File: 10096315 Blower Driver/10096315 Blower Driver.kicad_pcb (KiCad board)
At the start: 4 copper layers, 0 parts

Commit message: Created KiCad PCB Fie from Source
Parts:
- added ?: , , F.Cu at (266.1, 17.3)
- added ?: , , F.Cu at (266.6, 36.6)
- added ?: , , F.Cu at (278.6, 36.6)
- added ?: , , F.Cu at (290.4, 36.6)
- added ?: , , F.Cu at (291.6, 19.9)
- added ?: , , F.Cu at (295.0, 19.4)
- added C1: C-BC-C0805, C0805_1, F.Cu at (258.4, 23.7)
- added C10: C-BC-C1206, RC1206_1, F.Cu at (271.8, 63.4)
- added C11: C-BC-C0603, C0603_1, F.Cu at (267.0, 66.3)
- added C12: C-BC-C0805, C0805_2, F.Cu at (288.3, 57.7)
- added C13: C-BC-C1206, RC1206_1, F.Cu at (283.8, 63.4)
- added C14: C-BC-C0603, C0603_1, F.Cu at (279.1, 66.3)
- added C15: C-BC-C0805, C0805_2, F.Cu at (300.3, 57.7)
- added C16: C-BC-C1206, RC1206_1, F.Cu at (295.6, 63.4)
- added C17: C-BC-C0603, C0603_1, F.Cu at (290.8, 66.3)
- added C18: C-BC-C0805, C0805_1, F.Cu at (326.7, 40.2)
- added C19: C-BC-C0805, C0805_2, F.Cu at (309.6, 47.2)
- added C2: C-BTP-803, 03515_1, F.Cu at (305.8, 19.3)
- added C20: C-BC-C0603, C0603_1, F.Cu at (326.7, 42.5)
- added C21: C-BC-C0805, C0805_1, F.Cu at (317.8, 37.7)
- added C22: CC-BC-C0612, C0612-4_1, F.Cu at (299.4, 11.7)
- added C23: CC-BC-C0612, C0612-4_1, F.Cu at (309.2, 11.7)
- added C24: C-BC-C0805, C0805_1, F.Cu at (274.0, 45.3)
- added C25: C-BC-C0805, C0805_1, F.Cu at (286.1, 45.3)
- added C26: C-BC-C0805, C0805_1, F.Cu at (298.1, 45.3)
- added C27: C-BTP-803, 03515_1, F.Cu at (305.8, 30.1)
- added C28: C-BTP-HT1327, HT-13X27_1, F.Cu at (267.8, 19.5)
- added C29: C-BTP-HT1327, HT-13X27_1, F.Cu at (267.8, 6.51)
- added C3: C-BC-C0805, C0805_2, F.Cu at (299.1, 24.1)
- added C4: C-BCP-C7343, C7343_1, F.Cu at (271.8, 28.8)
- added C5: C-BC-C0805, C0805_2, F.Cu at (297.2, 28.8)
- added C6: C-BC-C0805, C0805_2, F.Cu at (315.9, 64.7)
- added C7: C-BC-C0603, C0603_1, F.Cu at (309.6, 59.6)
- added C8: C-BC-C0603, C0603_1, F.Cu at (309.6, 57.7)
- added C9: C-BC-C0805, C0805_2, F.Cu at (276.2, 57.7)
- added CAM14: FEE_COMP, FEE_COMP_1, B.Cu at (247.0, 71.1)
- added CAM15: FEE_COMP, FEE_COMP_1, F.Cu at (315.0, 71.1)
- added CAM5: FILM18_HORIZONTAL, FILM18_HORIZONTAL_1, F.Cu at (288.3, 42.0)
- added D1: D-BC-SMB, SMB_1, F.Cu at (291.5, 28.2)
- added D10: D-BC-SMA, SMA_1, F.Cu at (288.6, 51.4)
- added D11: D-BC-SOD80, SOD80_1, F.Cu at (271.8, 66.3)
- added D12: D-BC-SOD80, SOD80_1, F.Cu at (283.8, 66.3)
- added D13: D-BC-SOD80, SOD80_1, F.Cu at (295.6, 66.3)
- added D14: D-BC-SOT23, SOT23-1G_1, F.Cu at (267.0, 63.4)
- added D15: D-BC-SOT23, SOT23-1G_1, F.Cu at (279.1, 63.4)
- added D16: D-BC-SOT23, SOT23-1G_1, F.Cu at (290.8, 63.4)
- added D17: D-BC-DPAK-2ANODES, DPAK-2ANODES_1, B.Cu at (274.3, 11.4)
- added D18: D-BC-SMB, SMB_1, F.Cu at (268.3, 45.3)
- added D19: D-BC-SMB, SMB_2, F.Cu at (270.8, 37.1)
- added D2: D-BC-SOD323, SOD323_1, F.Cu at (270.8, 60.3)
- added D20: D-BC-SMB, SMB_1, F.Cu at (280.4, 45.3)
- added D21: D-BC-SMB, SMB_2, F.Cu at (282.9, 37.1)
- added D22: D-BC-SMB, SMB_1, F.Cu at (292.4, 45.3)
- added D23: D-BC-SMB, SMB_2, F.Cu at (295.0, 37.1)
- added D24: D-BC-SOT23, SOT23-1G_2, F.Cu at (285.7, 28.5)
- added D3: D-BC-SOD323, SOD323_1, F.Cu at (282.9, 60.3)
- added D4: D-BC-SOD323, SOD323_1, F.Cu at (295.0, 60.3)
- added D5: D-BC-SOD323, SOD323_1, F.Cu at (273.0, 33.6)
- added D6: D-BC-SOD323, SOD323_1, F.Cu at (284.8, 33.6)
- added D7: D-BC-SOD323, SOD323_1, F.Cu at (296.9, 33.6)
- added D8: D-BC-SMA, SMA_1, F.Cu at (265.1, 51.0)
- added D9: D-BC-SMA, SMA_1, F.Cu at (276.5, 51.0)
- added F1: FU-BC-154000, FU154000_1, F.Cu at (261.0, 28.8)
- added FI1: FL-10-BNX002-01, BNX002_1, F.Cu at (248.9, 26.0)
- added FI3: SF-BC-S0603, C0603_1, F.Cu at (302.9, 11.4)
- added FI4: SF-BC-S0603, C0603_1, F.Cu at (304.8, 11.4)
- added FI5: SF-BC-S0603, C0603_1, F.Cu at (306.7, 11.4)
- added FI6: SF-BC-S0603, C0603_1, F.Cu at (319.1, 11.4)
- added FI7: SF-BC-S0603, C0603_1, F.Cu at (317.2, 11.4)
- added FI8: SF-BC-S0603, C0603_1, F.Cu at (315.3, 11.4)
- added FI9: SF-BC-S0603, C0603_1, F.Cu at (313.4, 11.4)
- added IC1: L-BC-SO24, MX.A24_COMPOSANT_1, F.Cu at (317.8, 47.6)
- added IC2: L-BC-SO08, MX.A8_COMPOSANT_1, F.Cu at (315.9, 60.6)
- added IC3: L-BC-SO08, MX.A8_COMPOSANT_1, F.Cu at (270.5, 56.1)
- added IC4: L-BC-SO08, MX.A8_COMPOSANT_1, F.Cu at (282.6, 56.1)
- added IC5: L-BC-SO08, MX.A8_COMPOSANT_1, F.Cu at (294.6, 56.1)
- added IC6: REG-BC-DPAK, DPAK_1, B.Cu at (292.7, 10.1)
- added J1: F-COCMS-MOL43650-0212, MOL43650-02C_1, F.Cu at (261.3, 19.7)
- added J11: F-CO-MOL5566-02, MOL5566-2_1, F.Cu at (243.8, 16.7)
- added J2: F-CO-HE10-2010D, BP2X5D_1, F.Cu at (314.8, 4.05)
- added J22: F-CO-MOL7395M09, MOL7395-9_1, F.Cu at (313.8, 14.2)
- added J3: F-CO-MOL7395M02, MOL7395-2_1, F.Cu at (261.3, 56.4)
- added J6: F-CO-MOL7395M08, MOL7395-8_1, F.Cu at (261.3, 51.4)
- added MIR1: MIRECMS, MIRECMS-SAFT_1, F.Cu at (243.8, 2.47)
- added MIR2: MIRECMS, MIRECMS-SAFT_1, F.Cu at (330.5, 69.1)
- added MIR3: MIRECMS, MIRECMS-SAFT_1, B.Cu at (331.5, 5.32)
- added MIR4: MIRECMS, MIRECMS-SAFT_1, B.Cu at (249.9, 69.8)
- added PT1: PT-CMS-C12000, C12000_1, F.Cu at (328.9, 2.14)
- added R1: R-BC-R2512, R2512_1, F.Cu at (305.4, 42.1)
- added R10: R-BC-R0603, R0603_1, F.Cu at (295.6, 69.1)
- added R11: R-BC-R0603, R0603_1, F.Cu at (267.3, 60.3)
- added R12: R-BC-R0603, R0603_1, F.Cu at (279.4, 60.3)
- added R13: R-BC-R0603, R0603_1, F.Cu at (291.5, 60.3)
- added R2: R-BC-R0603, R0603_1, F.Cu at (309.6, 49.5)
- added R20: R-BC-R0603, R0603_1, F.Cu at (295.0, 52.3)
- added R3: R-BC-R0603, R0603_1, F.Cu at (278.1, 27.5)
- added R30: R-BC-R0603, R0603_1, F.Cu at (293.1, 33.6)
- added R31: R-BC-R0603, R0603_1, F.Cu at (269.2, 33.6)
- added R32: R-BC-R0603, R0603_1, F.Cu at (282.9, 52.3)
- added R33: R-BC-R0603, R0603_1, F.Cu at (281.0, 33.6)
- added R35: R-BC-R0603, R0603_1, F.Cu at (270.8, 52.3)
- added R37: R-BC-R0603, R0603_1, F.Cu at (309.6, 61.5)
- added R38: R-BC-R0603, R0603_1, F.Cu at (305.4, 45.3)
- added R39: R-BC-R0603, R0603_1, F.Cu at (311.8, 37.7)
- added R4: R-BC-R0603, R0603_1, F.Cu at (266.1, 23.7)
- added R40: R-BC-R2512, R2512_1, F.Cu at (305.4, 38.0)
- added R41: R-BC-R0603, R0603_1, F.Cu at (326.7, 44.7)
- added R42: R-BC-R0603, R0603_1, F.Cu at (326.7, 38.0)
- added R5: R-BC-R0603, R0603_1, F.Cu at (326.7, 46.6)
- added R50: R-BC-R0603, R0603_1, F.Cu at (309.6, 63.4)
- added R58: R-BC-R1206, RC1206_1, F.Cu at (275.3, 60.3)
- added R59: R-BC-R1206, RC1206_1, F.Cu at (287.3, 60.3)
- added R6: R-BC-R0603, R0603_1, F.Cu at (271.8, 69.1)
- added R60: R-BC-R1206, RC1206_1, F.Cu at (299.4, 60.3)
- added R7: R-BC-R0603, R0603_1, F.Cu at (329.6, 38.0)
- added R8: R-BC-R0603, R0603_1, F.Cu at (326.7, 48.5)
- added R9: R-BC-R0603, R0603_1, F.Cu at (283.8, 69.1)
- added T1: Q-SOT23-IRLML2803, SOT23-GSD_1, F.Cu at (309.6, 53.3)
- added T10: Q-SOT23-IRLML2803, SOT23-GSD_2, F.Cu at (281.9, 28.5)
- added T2: Q-BC-DPAK-GDS, DPAK-GDS_1, B.Cu at (270.5, 58.7)
- added T3: Q-BC-DPAK-GDS, DPAK-GDS_1, B.Cu at (270.5, 31.7)
- added T4: Q-BC-DPAK-GDS, DPAK-GDS_1, B.Cu at (282.6, 58.7)
- added T5: Q-BC-DPAK-GDS, DPAK-GDS_1, B.Cu at (282.6, 31.7)
- added T6: Q-BC-DPAK-GDS, DPAK-GDS_1, B.Cu at (294.6, 58.7)
- added T7: Q-BC-DPAK-GDS, DPAK-GDS_1, B.Cu at (294.6, 31.7)
- added T8: Q-SOT23-IRLML2803, SOT23-GSD_2, F.Cu at (326.7, 51.7)
- added T9: Q-BC-DPAK-GDS, DPAK-GDS_1, B.Cu at (261.0, 9.76)
- added ZC2: C-BCP-WX8, C-SC8_1, F.Cu at (305.4, 19.3)
- added ZC27: C-BCP-WX10, C-SC10_1, F.Cu at (305.8, 30.1)
- added ZM1: FIX-0035M, FIX35M_1, F.Cu at (250.3, 63.0)
- added ZM2: FIX-0035M, FIX35M_1, F.Cu at (324.9, 63.0)
- added ZM3: FIX-0035M, FIX35M_1, F.Cu at (324.9, 8.80)
- added ZM4: FIX-0035M, FIX35M_1, F.Cu at (250.3, 8.80)
- added ZT2: Q-BT-TO220AB-GDS-INV, TO220ABGDS-INV_COUCHE_1, B.Cu at (270.5, 67.5)
- added ZT3: Q-BT-TO220AB-GDS-INV, TO220ABGDS-INV_COUCHE_1, B.Cu at (270.5, 23.1)
- added ZT4: Q-BT-TO220AB-GDS-INV, TO220ABGDS-INV_COUCHE_1, B.Cu at (282.6, 67.5)
- added ZT5: Q-BT-TO220AB-GDS-INV, TO220ABGDS-INV_COUCHE_1, B.Cu at (282.6, 23.1)
- added ZT6: Q-BT-TO220AB-GDS-INV, TO220ABGDS-INV_COUCHE_1, B.Cu at (294.6, 67.5)
- added ZT7: Q-BT-TO220AB-GDS-INV, TO220ABGDS-INV_COUCHE_1, B.Cu at (294.6, 23.1)
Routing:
- net (no net): track 0.00 -> 3049.6 mm, vias 0 -> 81
- added copper zone on B.Cu, net (none)
- added copper zone on F.Cu, net (none)
- added copper zone on In1.Cu, net (none)
- added copper zone on In2.Cu, net (none)
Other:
- board outline added: 92.5 x 72 mm
- net class Default: clearance 0.1524 -> 0.2; trace_width 0.254 -> 0.25; via_dia 0.6858 -> 0.8; via_drill 0.3302 -> 0.4
- rule pad_to_mask_clearance: 0 -> 0.051
- rule solder_mask_min_width: 0.1016 -> 0.25
- rule trace_clearance: 0.1524 -> 0.2
- rule trace_min: 0.127 -> 0.2
- rule via_min_drill: 0.254 -> 0.3
- rule via_min_size: 0.4572 -> 0.4
- board text added: "+"
- board text added: "-"
- board text added: "1"
- board text added: "10096505"
- board text added: "2"
- board text added: "21"
- board text added: "3"
- board text added: "4"
- board text added: "BRAKE/"
- board text added: "CDE TURBINE RB0505"
- board text added: "EN"
- board text added: "FAULT/"
- board text added: "GND"
- board text added: "IDENT"
- board text added: "J4"
- board text added: "L1"
- board text added: "NC"
- board text added: "PH1"
- board text added: "PH2"
- board text added: "PH3"
- board text added: "SENS1"
- board text added: "SENS2"
- board text added: "SENS3"
- board text added: "SPD-MEA"
- board text added: "SPD-SET"
- board text added: "SUPPLY"

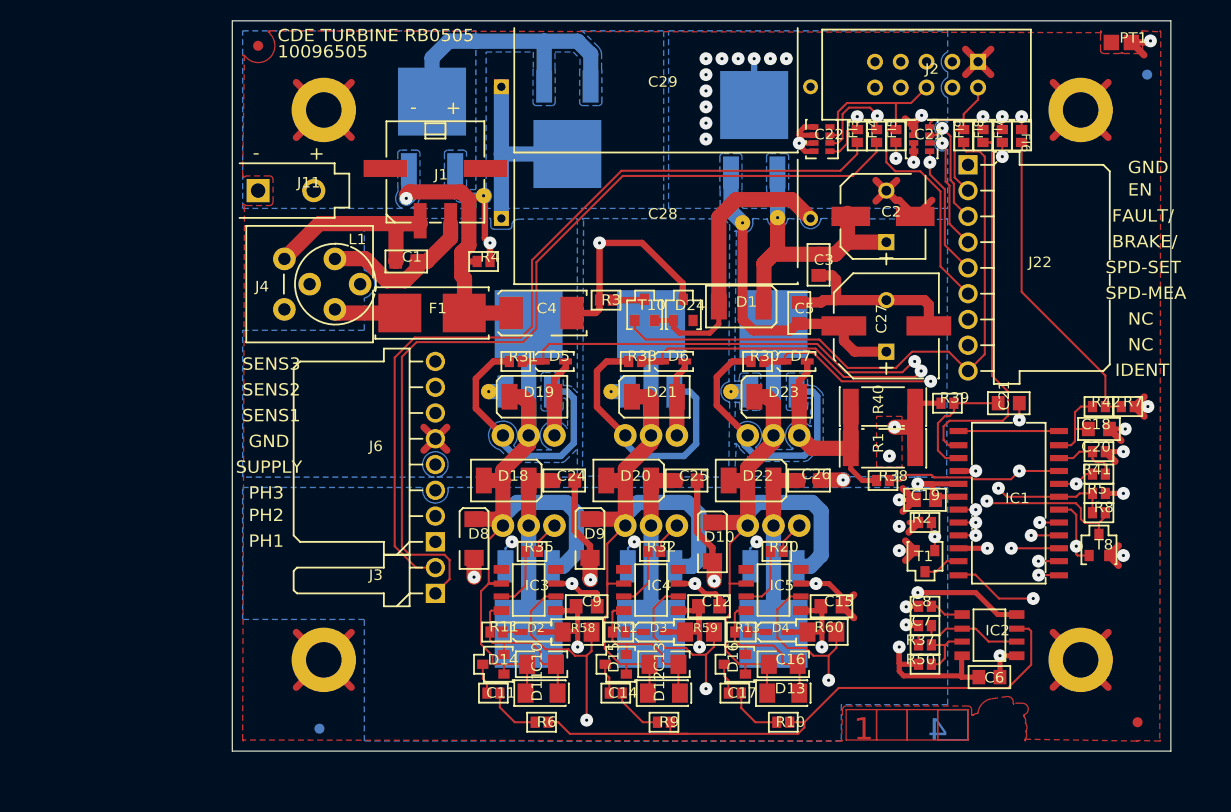
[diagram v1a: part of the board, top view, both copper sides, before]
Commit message: Updated with George's exported PCB. Fixed pin-pad associations. Still need net-tie placement and to fix one weird issue with pad 2 of J4 not being recognized
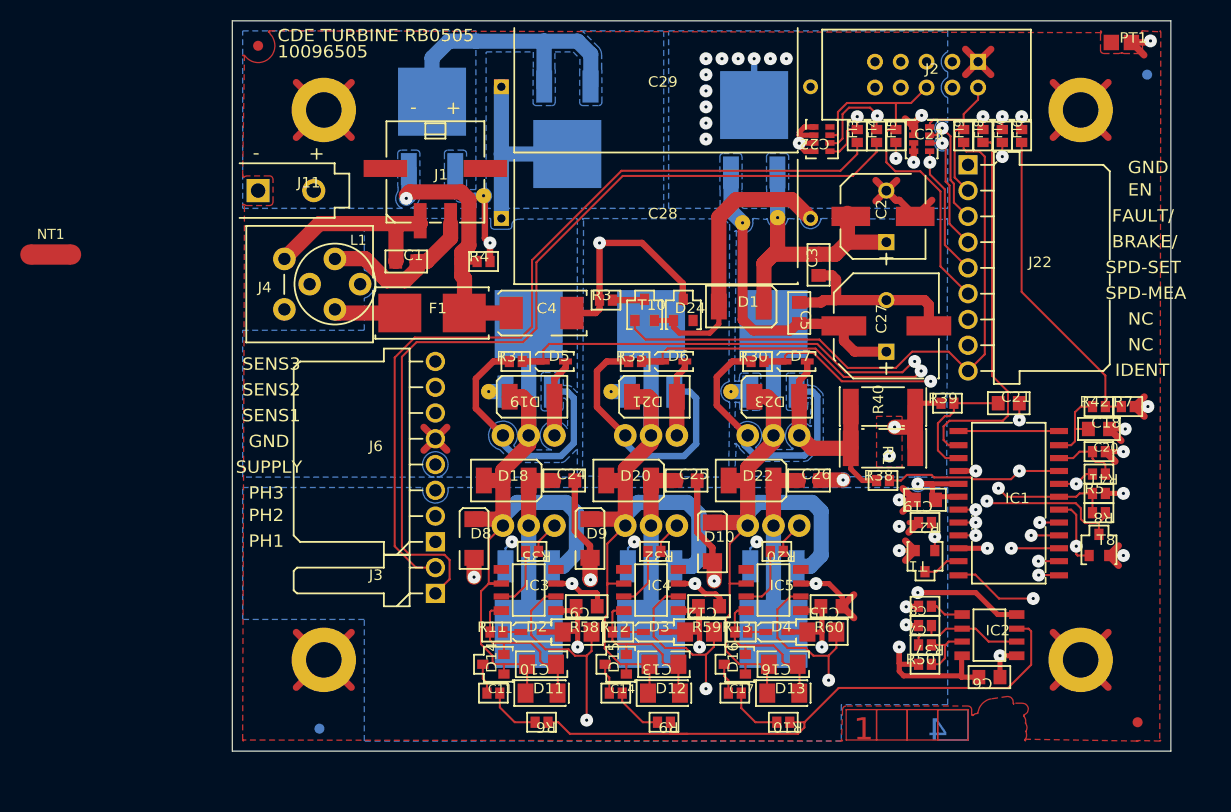
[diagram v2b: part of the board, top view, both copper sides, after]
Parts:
- added J4: JumperBypass, 10096315 Blower Driver:JUMPER2_NoCopper, F.Cu at (246.4, 26.0)
- added L1: Inductor_22uH, 10096315 Blower Driver:ELC09DxxxxF_NoCopper, F.Cu at (251.4, 26.0)
- added NT1: Net-Tie_2, NetTie:NetTie-2_SMD_Pad2.0mm, F.Cu at (223.4, 23.0)
- C1, C21, C24, C25, C26: value C-BC-C0805 -> Capacitor_100nF; footprint C0805_1 -> 10096315 Blower Driver:C0805
- C10, C13, C16: value C-BC-C1206 -> Capacitor_220nF; footprint RC1206_1 -> 10096315 Blower Driver:RC1206
- C11, C14, C17, C7: value C-BC-C0603 -> Capacitor_2.2nF; footprint C0603_1 -> 10096315 Blower Driver:C0603
- C12, C15, C19, C3, C5, C6, C9: value C-BC-C0805 -> Capacitor_100nF; footprint C0805_2 -> 10096315 Blower Driver:C0805
- C18: value C-BC-C0805 -> Capacitor_330nF; footprint C0805_1 -> 10096315 Blower Driver:C0805
- C2: value C-BTP-803 -> Capacitor_100uF_CheckFootprint; footprint 03515_1 -> 10096315 Blower Driver:03515
- C20, C8: value C-BC-C0603 -> Capacitor_10nF; footprint C0603_1 -> 10096315 Blower Driver:C0603
- C22, C23: value CC-BC-C0612 -> CapacitorArray_47pf; footprint C0612-4_1 -> 10096315 Blower Driver:C0612-4
- C27: value C-BTP-803 -> Capacitor_470uF_CheckFootprint; footprint 03515_1 -> 10096315 Blower Driver:03515
- C28, C29: value C-BTP-HT1327 -> Capacitor_1000uF; footprint HT-13X27_1 -> 10096315 Blower Driver:HT-13X27
- C4: value C-BCP-C7343 -> Capacitor_22uF_CheckFootprint; footprint C7343_1 -> 10096315 Blower Driver:C7343
- D1, D18, D20, D22: value D-BC-SMB -> DiodeZener_30V; footprint SMB_1 -> 10096315 Blower Driver:SMB
- D10, D8, D9: value D-BC-SMA -> DiodeZener_200V; footprint SMA_1 -> 10096315 Blower Driver:SMA
- D11, D12, D13: value D-BC-SOD80 -> DiodeZener_30V; footprint SOD80_1 -> 10096315 Blower Driver:SOD80
- D14, D15, D16: value D-BC-SOT23 -> DiodeSchottkySeriesPair; footprint SOT23-1G_1 -> 10096315 Blower Driver:SOT23-1G
- D17: value D-BC-DPAK-2ANODES -> DiodeSchottkyParallelPair; footprint DPAK-2ANODES_1 -> 10096315 Blower Driver:DPAK-2ANODES
- D19, D21, D23: value D-BC-SMB -> DiodeZener_30V; footprint SMB_2 -> 10096315 Blower Driver:SMB
- D2, D3, D4, D5, D6, D7: value D-BC-SOD323 -> DiodeSchottky; footprint SOD323_1 -> 10096315 Blower Driver:SOD323
- D24: value D-BC-SOT23 -> DiodeSchottkySeriesPair; footprint SOT23-1G_2 -> 10096315 Blower Driver:SOT23-1G
- F1: value FU-BC-154000 -> Fuse_5A; footprint FU154000_1 -> 10096315 Blower Driver:FU154000
- FI1: value FL-10-BNX002-01 -> FilterBNX002011; footprint BNX002_1 -> 10096315 Blower Driver:BNX002
- FI3, FI4, FI5, FI6, FI7, FI8, FI9: value SF-BC-S0603 -> FerriteBead; footprint C0603_1 -> 10096315 Blower Driver:C0603
- IC1: value L-BC-SO24 -> MotorDriver; footprint MX.A24_COMPOSANT_1 -> 10096315 Blower Driver:MX.A24_COMPOSANT
- IC2: value L-BC-SO08 -> NE555D; footprint MX.A8_COMPOSANT_1 -> 10096315 Blower Driver:MX.A8_COMPOSANT
- IC3, IC4, IC5: value L-BC-SO08 -> HighSideDriver; footprint MX.A8_COMPOSANT_1 -> 10096315 Blower Driver:MX.A8_COMPOSANT
- IC6: value REG-BC-DPAK -> LinearRegulator; footprint DPAK_1 -> 10096315 Blower Driver:DPAK
- J1: value F-COCMS-MOL43650-0212 -> 2pinConnector_Power; footprint MOL43650-02C_1 -> 10096315 Blower Driver:MOL43650-02C
- J11: value F-CO-MOL5566-02 -> 2pinConnector_Unknown; footprint MOL5566-2_1 -> 10096315 Blower Driver:MOL5566-2
- J2: value F-CO-HE10-2010D -> 10pinConnector; footprint BP2X5D_1 -> 10096315 Blower Driver:BP2X5D
- J22: value F-CO-MOL7395M09 -> 9pinConnector; footprint MOL7395-9_1 -> 10096315 Blower Driver:MOL7395-9
- J3: value F-CO-MOL7395M02 -> 2pinConnector; footprint MOL7395-2_1 -> 10096315 Blower Driver:MOL7395-2
- J6: value F-CO-MOL7395M08 -> 8pinConnector; footprint MOL7395-8_1 -> 10096315 Blower Driver:MOL7395-8
- MIR1, MIR2, MIR3, MIR4: value MIRECMS -> Fiducial; footprint MIRECMS-SAFT_1 -> 10096315 Blower Driver:MIRECMS-SAFT
- PT1: value PT-CMS-C12000 -> TestPoint; footprint C12000_1 -> 10096315 Blower Driver:C12000
- R1: value R-BC-R2512 -> Resistor_0R047; footprint R2512_1 -> 10096315 Blower Driver:R2512
- R10, R6, R9: value R-BC-R0603 -> Resistor_680R; footprint R0603_1 -> 10096315 Blower Driver:R0603
- R11, R12, R13: value R-BC-R0603 -> Resistor_100R; footprint R0603_1 -> 10096315 Blower Driver:R0603
- R2, R37, R42, R5: value R-BC-R0603 -> Resistor_10k; footprint R0603_1 -> 10096315 Blower Driver:R0603
- R20, R30, R31, R32, R33, R35: value R-BC-R0603 -> Resistor_10R; footprint R0603_1 -> 10096315 Blower Driver:R0603
- R3, R4, R7: value R-BC-R0603 -> Resistor_100k; footprint R0603_1 -> 10096315 Blower Driver:R0603
- R38, R39, R50: value R-BC-R0603 -> Resistor_1k; footprint R0603_1 -> 10096315 Blower Driver:R0603
- R40: value R-BC-R2512 -> Resistor_0R100; footprint R2512_1 -> 10096315 Blower Driver:R2512
- R41: value R-BC-R0603 -> Resistor_22k; footprint R0603_1 -> 10096315 Blower Driver:R0603
- R58, R59, R60: value R-BC-R1206 -> Resistor_1k_0.5W; footprint RC1206_1 -> 10096315 Blower Driver:RC1206
- R8: value R-BC-R0603 -> Resistor_4k7; footprint R0603_1 -> 10096315 Blower Driver:R0603
- T1: value Q-SOT23-IRLML2803 -> MOSFET_NMOS_30V; footprint SOT23-GSD_1 -> 10096315 Blower Driver:SOT23-GSD
- T10: value Q-SOT23-IRLML2803 -> MOSFET_NMOS_30V; footprint SOT23-GSD_2 -> 10096315 Blower Driver:SOT23-GSD
- T2, T3, T4, T5, T7: value Q-BC-DPAK-GDS -> MOSFET_NMOS_55V; footprint DPAK-GDS_1 -> 10096315 Blower Driver:DPAK-GDS
- T6: value Q-BC-DPAK-GDS -> MOSFET_NMOS_30V; footprint DPAK-GDS_1 -> 10096315 Blower Driver:DPAK-GDS
- T8: value Q-SOT23-IRLML2803 -> MOSFET_NMOS_55V; footprint SOT23-GSD_2 -> 10096315 Blower Driver:SOT23-GSD
- T9: value Q-BC-DPAK-GDS -> MOSFET_PMOS_60V; footprint DPAK-GDS_1 -> 10096315 Blower Driver:DPAK-GDS
- ZM1, ZM2, ZM3, ZM4: value FIX-0035M -> MountingHole_Pad; footprint FIX35M_1 -> 10096315 Blower Driver:FIX35M
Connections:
- C1 pad 1: (no net) -> Net-(C1-Pad1)
- C1 pad 2: (no net) -> Net-(C1-Pad2)
- C10 pad 1: (no net) -> Net-(C10-Pad1)
- C10 pad 2: (no net) -> Net-(C10-Pad2)
- C11 pad 1: (no net) -> Net-(C11-Pad1)
- C11 pad 2: (no net) -> Net-(C11-Pad2)
- C12 pad 1: (no net) -> +15V
- C12 pad 2: (no net) -> GND
- C13 pad 1: (no net) -> Net-(C13-Pad1)
- C13 pad 2: (no net) -> Net-(C13-Pad2)
- C14 pad 1: (no net) -> Net-(C14-Pad1)
- C14 pad 2: (no net) -> Net-(C14-Pad2)
- C15 pad 1: (no net) -> +15V
- C15 pad 2: (no net) -> GND
- C16 pad 1: (no net) -> Net-(C16-Pad1)
- C16 pad 2: (no net) -> Net-(C16-Pad2)
- C17 pad 1: (no net) -> Net-(C17-Pad1)
- C17 pad 2: (no net) -> Net-(C17-Pad2)
- C18 pad 1: (no net) -> Net-(C18-Pad1)
- C18 pad 2: (no net) -> GND
- C19 pad 1: (no net) -> GND
- C19 pad 2: (no net) -> +15V
- C2 pad +: (no net) -> GND
- C2 pad -: (no net) -> +24V
- C20 pad 1: (no net) -> Net-(C20-Pad1)
- C20 pad 2: (no net) -> GND
- C21 pad 1: (no net) -> Net-(C21-Pad1)
- C21 pad 2: (no net) -> Net-(C21-Pad2)
- C22 pad 1: (no net) -> Net-(C22-Pad1)
- C22 pad 2: (no net) -> Net-(C22-Pad2)
- C22 pad 3: (no net) -> Net-(C22-Pad3)
- C22 pad 4: (no net) -> Net-(C22-Pad4)
- C22 pad 5: (no net) -> GND
- C22 pad 6: (no net) -> GND
- C22 pad 7: (no net) -> GND
- C22 pad 8: (no net) -> GND
- C23 pad 1: (no net) -> GND
- C23 pad 2: (no net) -> GND
- C23 pad 3: (no net) -> GND
- C23 pad 4: (no net) -> GND
- C23 pad 5: (no net) -> Net-(C23-Pad5)
- C23 pad 6: (no net) -> Net-(C23-Pad6)
- C23 pad 7: (no net) -> Net-(C23-Pad7)
- C23 pad 8: (no net) -> Net-(C23-Pad8)
- C24 pad 1: (no net) -> GNDPWR
- C24 pad 2: (no net) -> +24V
- C25 pad 1: (no net) -> GNDPWR
- C25 pad 2: (no net) -> +24V
- C26 pad 1: (no net) -> GNDPWR
- C26 pad 2: (no net) -> +24V
- C27 pad +: (no net) -> +15V
- C27 pad -: (no net) -> GND
- C28 pad +: (no net) -> +24V
- C28 pad -: (no net) -> GNDPWR
- C29 pad +: (no net) -> +24V
- C29 pad -: (no net) -> GNDPWR
- C3 pad 1: (no net) -> +24V
- C3 pad 2: (no net) -> GND
- C4 pad +: (no net) -> Net-(C4-Pad+)
- C4 pad -: (no net) -> Net-(C4-Pad-)
- C5 pad 1: (no net) -> +15V
- C5 pad 2: (no net) -> GND
- C6 pad 1: (no net) -> +15V
- C6 pad 2: (no net) -> GND
- C7 pad 1: (no net) -> Net-(C7-Pad1)
- C7 pad 2: (no net) -> GND
- C8 pad 1: (no net) -> Net-(C8-Pad1)
- C8 pad 2: (no net) -> GND
- C9 pad 1: (no net) -> +15V
- C9 pad 2: (no net) -> GND
- D1 pad A: (no net) -> GNDPWR
- D1 pad K: (no net) -> +24V
- D10 pad A: (no net) -> GNDPWR
- D10 pad K: (no net) -> Net-(C16-Pad2)
- D11 pad A: (no net) -> Net-(C10-Pad2)
- D11 pad K: (no net) -> Net-(C10-Pad1)
- D12 pad A: (no net) -> Net-(C13-Pad2)
- D12 pad K: (no net) -> Net-(C13-Pad1)
- D13 pad A: (no net) -> Net-(C16-Pad2)
- D13 pad K: (no net) -> Net-(C16-Pad1)
- D14 pad 1: (no net) -> Net-(C10-Pad2)
- D14 pad 2: (no net) -> Net-(C10-Pad1)
- D14 pad 3: (no net) -> Net-(C11-Pad2)
- D15 pad 1: (no net) -> Net-(C13-Pad2)
- D15 pad 2: (no net) -> Net-(C13-Pad1)
- D15 pad 3: (no net) -> Net-(C14-Pad2)
- D16 pad 1: (no net) -> Net-(C16-Pad2)
- D16 pad 2: (no net) -> Net-(C16-Pad1)
- D16 pad 3: (no net) -> Net-(C17-Pad2)
- D17 pad A1: (no net) -> Net-(D17-PadA1)
- D17 pad A2: (no net) -> Net-(D17-PadA1)
- D17 pad K: (no net) -> +24V
- D18 pad A: (no net) -> Net-(D18-PadA)
- D18 pad K: (no net) -> +24V
- D19 pad A: (no net) -> /ISENS
- D19 pad K: (no net) -> Net-(D18-PadA)
- D2 pad A: (no net) -> +15V
- D2 pad K: (no net) -> Net-(D2-PadK)
- D20 pad A: (no net) -> Net-(D20-PadA)
- D20 pad K: (no net) -> +24V
- D21 pad A: (no net) -> /ISENS
- D21 pad K: (no net) -> Net-(D20-PadA)
- D22 pad A: (no net) -> Net-(D22-PadA)
- D22 pad K: (no net) -> +24V
- D23 pad A: (no net) -> /ISENS
- D23 pad K: (no net) -> Net-(D22-PadA)
- D24 pad 1: (no net) -> GNDPWR
- D24 pad 2: (no net) -> Net-(D24-Pad2)
- D24 pad 3: (no net) -> Net-(C4-Pad-)
- D3 pad A: (no net) -> +15V
- D3 pad K: (no net) -> Net-(D3-PadK)
- D4 pad A: (no net) -> +15V
- D4 pad K: (no net) -> Net-(D4-PadK)
- D5 pad A: (no net) -> /ISENS
- D5 pad K: (no net) -> /BOT-DR-C
- D6 pad A: (no net) -> /ISENS
- D6 pad K: (no net) -> /BOT-DR-B
- D7 pad A: (no net) -> /ISENS
- D7 pad K: (no net) -> /BOT-DR-A
- D8 pad A: (no net) -> GNDPWR
- D8 pad K: (no net) -> Net-(C10-Pad2)
- D9 pad A: (no net) -> GNDPWR
- D9 pad K: (no net) -> Net-(C13-Pad2)
- F1 pad 1: (no net) -> Net-(C4-Pad+)
- F1 pad 2: (no net) -> Net-(F1-Pad2)
- FI1 pad B: (no net) -> Net-(C1-Pad1)
- FI1 pad CB: (no net) -> Net-(F1-Pad2)
- FI1 pad CG1: (no net) -> GNDPWR
- FI1 pad CG2: (no net) -> GNDPWR
- FI1 pad CG3: (no net) -> GNDPWR
- FI1 pad PSG: (no net) -> Net-(C1-Pad2)
- FI3 pad 1: (no net) -> /TEMP+
- FI3 pad 2: (no net) -> Net-(C22-Pad1)
- FI4 pad 1: (no net) -> /TEMP-
- FI4 pad 2: (no net) -> Net-(C22-Pad2)
- FI5 pad 1: (no net) -> Net-(FI5-Pad1)
- FI5 pad 2: (no net) -> Net-(C22-Pad3)
- FI6 pad 1: (no net) -> Net-(FI6-Pad1)
- FI6 pad 2: (no net) -> Net-(C23-Pad5)
- FI7 pad 1: (no net) -> Net-(FI7-Pad1)
- FI7 pad 2: (no net) -> Net-(C23-Pad6)
- FI8 pad 1: (no net) -> Net-(FI8-Pad1)
- FI8 pad 2: (no net) -> Net-(C23-Pad7)
- FI9 pad 1: (no net) -> /OE
- FI9 pad 2: (no net) -> Net-(C23-Pad8)
- IC1 pad 1: (no net) -> /TOP-DR-B
- IC1 pad 10: (no net) -> Net-(C20-Pad1)
- IC1 pad 11: (no net) -> Net-(C18-Pad1)
- IC1 pad 12: (no net) -> Net-(IC1-Pad12)
- IC1 pad 13: (no net) -> Net-(IC1-Pad12)
- IC1 pad 14: (no net) -> Net-(FI8-Pad1)
- IC1 pad 15: (no net) -> Net-(C21-Pad2)
- IC1 pad 16: (no net) -> GND
- IC1 pad 17: (no net) -> +15V
- IC1 pad 18: (no net) -> +15V
- IC1 pad 19: (no net) -> /BOT-DR-C
- IC1 pad 2: (no net) -> /TOP-DR-A
- IC1 pad 20: (no net) -> /BOT-DR-B
- IC1 pad 21: (no net) -> /BOT-DR-A
- IC1 pad 22: (no net) -> GND
- IC1 pad 23: (no net) -> Net-(IC1-Pad23)
- IC1 pad 24: (no net) -> /TOP-DR-C
- IC1 pad 3: (no net) -> /V-REF-M
- IC1 pad 4: (no net) -> /SENSOR1
- IC1 pad 5: (no net) -> /SENSOR2
- IC1 pad 6: (no net) -> /SENSOR3
- IC1 pad 7: (no net) -> /OE
- IC1 pad 8: (no net) -> /V-REF-M
- IC1 pad 9: (no net) -> Net-(C21-Pad1)
- IC2 pad 1: (no net) -> GND
- IC2 pad 2: (no net) -> Net-(C7-Pad1)
- IC2 pad 3: (no net) -> /OSC
- IC2 pad 4: (no net) -> +15V
- IC2 pad 5: (no net) -> Net-(C8-Pad1)
- IC2 pad 6: (no net) -> Net-(C7-Pad1)
- IC2 pad 7: (no net) -> Net-(IC2-Pad7)
- IC2 pad 8: (no net) -> +15V
- IC3 pad 1: (no net) -> +15V
- IC3 pad 2: (no net) -> /TOP-DR-C
- IC3 pad 3: (no net) -> GND
- IC3 pad 4: (no net) -> Net-(IC3-Pad4)
- IC3 pad 5: (no net) -> Net-(IC3-Pad5)
- IC3 pad 6: (no net) -> Net-(C10-Pad2)
- IC3 pad 7: (no net) -> Net-(IC3-Pad7)
- IC3 pad 8: (no net) -> Net-(C10-Pad1)
- IC4 pad 1: (no net) -> +15V
- IC4 pad 2: (no net) -> /TOP-DR-B
- IC4 pad 3: (no net) -> GND
- IC4 pad 4: (no net) -> Net-(IC4-Pad4)
- IC4 pad 5: (no net) -> Net-(IC4-Pad5)
- IC4 pad 6: (no net) -> Net-(C13-Pad2)
- IC4 pad 7: (no net) -> Net-(IC4-Pad7)
- IC4 pad 8: (no net) -> Net-(C13-Pad1)
- IC5 pad 1: (no net) -> +15V
- IC5 pad 2: (no net) -> /TOP-DR-A
- IC5 pad 3: (no net) -> GND
- IC5 pad 4: (no net) -> Net-(IC5-Pad4)
- IC5 pad 5: (no net) -> Net-(IC5-Pad5)
- IC5 pad 6: (no net) -> Net-(C16-Pad2)
- IC5 pad 7: (no net) -> Net-(IC5-Pad7)
- IC5 pad 8: (no net) -> Net-(C16-Pad1)
- IC6 pad 1: (no net) -> +24V
- IC6 pad 2: (no net) -> GND
- IC6 pad 3: (no net) -> +15V
- J1 pad 1: (no net) -> Net-(C1-Pad2)
- J1 pad 2: (no net) -> Net-(C1-Pad1)
- J11 pad 1: (no net) -> Net-(C1-Pad2)
- J11 pad 2: (no net) -> Net-(C1-Pad1)
- J2 pad 1: (no net) -> GND
- J2 pad 10: (no net) -> Net-(C22-Pad1)
- J2 pad 2: (no net) -> Net-(C23-Pad8)
- J2 pad 3: (no net) -> Net-(C23-Pad7)
- J2 pad 4: (no net) -> Net-(C23-Pad6)
- J2 pad 5: (no net) -> Net-(C23-Pad5)
- J2 pad 6: (no net) -> Net-(C22-Pad3)
- J2 pad 7: (no net) -> Net-(J2-Pad7)
- J2 pad 8: (no net) -> Net-(J2-Pad8)
- J2 pad 9: (no net) -> Net-(C22-Pad2)
- J22 pad 1: (no net) -> GND
- J22 pad 2: (no net) -> Net-(C23-Pad8)
- J22 pad 3: (no net) -> Net-(C23-Pad7)
- J22 pad 4: (no net) -> Net-(C23-Pad6)
- J22 pad 5: (no net) -> Net-(C23-Pad5)
- J22 pad 6: (no net) -> Net-(C22-Pad3)
- J22 pad 7: (no net) -> Net-(J22-Pad7)
- J22 pad 8: (no net) -> Net-(J22-Pad8)
- J22 pad 9: (no net) -> /OE
- J3 pad 1: (no net) -> /TEMP-
- J3 pad 2: (no net) -> /TEMP+
- J6 pad 1: (no net) -> Net-(D22-PadA)
- J6 pad 2: (no net) -> Net-(D20-PadA)
- J6 pad 3: (no net) -> Net-(D18-PadA)
- J6 pad 4: (no net) -> /V-REF-M
- J6 pad 5: (no net) -> GND
- J6 pad 6: (no net) -> /SENSOR1
- J6 pad 7: (no net) -> /SENSOR2
- J6 pad 8: (no net) -> /SENSOR3
- PT1 pad 1: (no net) -> GND
- R1 pad 1: (no net) -> /ISENS
- R1 pad 2: (no net) -> GNDPWR
- R10 pad 1: (no net) -> /OSC
- R10 pad 2: (no net) -> Net-(C17-Pad1)
- R11 pad 1: (no net) -> Net-(C10-Pad1)
- R11 pad 2: (no net) -> Net-(D2-PadK)
- R12 pad 1: (no net) -> Net-(C13-Pad1)
- R12 pad 2: (no net) -> Net-(D3-PadK)
- R13 pad 1: (no net) -> Net-(C16-Pad1)
- R13 pad 2: (no net) -> Net-(D4-PadK)
- R2 pad 1: (no net) -> Net-(FI7-Pad1)
- R2 pad 2: (no net) -> GND
- R20 pad 1: (no net) -> Net-(R20-Pad1)
- R20 pad 2: (no net) -> Net-(IC5-Pad7)
- R3 pad 1: (no net) -> Net-(C4-Pad-)
- R3 pad 2: (no net) -> Net-(R3-Pad2)
- R30 pad 1: (no net) -> Net-(R30-Pad1)
- R30 pad 2: (no net) -> /BOT-DR-A
- R31 pad 1: (no net) -> Net-(R31-Pad1)
- R31 pad 2: (no net) -> /BOT-DR-C
- R32 pad 1: (no net) -> Net-(R32-Pad1)
- R32 pad 2: (no net) -> Net-(IC4-Pad7)
- R33 pad 1: (no net) -> Net-(R33-Pad1)
- R33 pad 2: (no net) -> /BOT-DR-B
- R35 pad 1: (no net) -> Net-(R35-Pad1)
- R35 pad 2: (no net) -> Net-(IC3-Pad7)
- R37 pad 1: (no net) -> Net-(IC2-Pad7)
- R37 pad 2: (no net) -> Net-(C7-Pad1)
- R38 pad 1: (no net) -> /ISENS
- R38 pad 2: (no net) -> Net-(C21-Pad1)
- R39 pad 1: (no net) -> GNDPWR
- R39 pad 2: (no net) -> Net-(C21-Pad2)
- R4 pad 1: (no net) -> Net-(C4-Pad+)
- R4 pad 2: (no net) -> Net-(C4-Pad-)
- R40 pad 1: (no net) -> /ISENS
- R40 pad 2: (no net) -> GNDPWR
- R41 pad 1: (no net) -> /V-REF-M
- R41 pad 2: (no net) -> Net-(C20-Pad1)
- R42 pad 1: (no net) -> Net-(C18-Pad1)
- R42 pad 2: (no net) -> Net-(FI6-Pad1)
- R5 pad 1: (no net) -> /OE
- R5 pad 2: (no net) -> GND
- R50 pad 1: (no net) -> +15V
- R50 pad 2: (no net) -> Net-(IC2-Pad7)
- R58 pad 1: (no net) -> +15V
- R58 pad 2: (no net) -> /TOP-DR-C
- R59 pad 1: (no net) -> +15V
- R59 pad 2: (no net) -> /TOP-DR-B
- R6 pad 1: (no net) -> /OSC
- R6 pad 2: (no net) -> Net-(C11-Pad1)
- R60 pad 1: (no net) -> +15V
- R60 pad 2: (no net) -> /TOP-DR-A
- R7 pad 1: (no net) -> Net-(FI6-Pad1)
- R7 pad 2: (no net) -> GND
- R8 pad 1: (no net) -> /OE
- R8 pad 2: (no net) -> Net-(FI5-Pad1)
- R9 pad 1: (no net) -> /OSC
- R9 pad 2: (no net) -> Net-(C14-Pad1)
- T1 pad D: (no net) -> Net-(IC1-Pad23)
- T1 pad G: (no net) -> Net-(FI7-Pad1)
- T1 pad S: (no net) -> GND
- T10 pad D: (no net) -> Net-(R3-Pad2)
- T10 pad G: (no net) -> /OE
- T10 pad S: (no net) -> GNDPWR
- T2 pad D: (no net) -> +24V
- T2 pad G: (no net) -> Net-(R35-Pad1)
- T2 pad S: (no net) -> Net-(D18-PadA)
- T3 pad D: (no net) -> Net-(D18-PadA)
- T3 pad G: (no net) -> Net-(R31-Pad1)
- T3 pad S: (no net) -> /ISENS
- T4 pad D: (no net) -> +24V
- T4 pad G: (no net) -> Net-(R32-Pad1)
- T4 pad S: (no net) -> Net-(D20-PadA)
- T5 pad D: (no net) -> Net-(D20-PadA)
- T5 pad G: (no net) -> Net-(R33-Pad1)
- T5 pad S: (no net) -> /ISENS
- T6 pad D: (no net) -> Net-(FI5-Pad1)
- T6 pad G: (no net) -> /SENSOR3
- T6 pad S: (no net) -> GND
- T7 pad D: (no net) -> Net-(D22-PadA)
- T7 pad G: (no net) -> Net-(R30-Pad1)
- T7 pad S: (no net) -> /ISENS
- T8 pad D: (no net) -> +24V
- T8 pad G: (no net) -> Net-(R20-Pad1)
- T8 pad S: (no net) -> Net-(D22-PadA)
- T9 pad D: (no net) -> Net-(D17-PadA1)
- T9 pad G: (no net) -> Net-(C4-Pad-)
- T9 pad S: (no net) -> Net-(C4-Pad+)
- ZM1 pad 1: (no net) -> GND
- ZM2 pad 1: (no net) -> GND
- ZM3 pad 1: (no net) -> GND
- ZM4 pad 1: (no net) -> GND
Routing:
- net (no net): track 3049.6 -> 2389.6 mm, vias 81 -> 59
- net GND: track 0.00 -> 188.6 mm, vias 0 -> 9
- net /V-REF-M: track 0.00 -> 100.7 mm, vias 0 -> 2
- net /SENSOR2: track 0.00 -> 99.0 mm, vias 0 -> 1
- net /SENSOR1: track 0.00 -> 94.1 mm, vias 0 -> 1
- net GNDPWR: track 0.00 -> 69.1 mm, vias 0 -> 1
- net Net-(C23-Pad5): track 0.00 -> 28.8 mm
- net Net-(D17-PadA1): track 0.00 -> 28.8 mm
- net Net-(IC1-Pad12): track 0.00 -> 9.91 mm
- net +15V: track 0.00 -> 4.71 mm, vias 0 -> 1
- net Net-(D22-PadA): track 0.00 -> 4.20 mm, vias 0 -> 1
- net Net-(FI6-Pad1): track 0.00 -> 4.11 mm, vias 0 -> 1
- net Net-(IC1-Pad23): track 0.00 -> 3.73 mm
- net Net-(C4-Pad-): track 0.00 -> 3.21 mm
- net Net-(C20-Pad1): track 0.00 -> 3.14 mm, vias 0 -> 1
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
